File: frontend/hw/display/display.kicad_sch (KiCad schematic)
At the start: 14 parts, among them J1 Conn_01x06, J3 Conn_01x04, Q1 MMBT3904, Q2 MMBT3904, U1 ESP32-WROOM-32U, U3 CH340C, U5 AMS1117-3.3

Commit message: Start connecting display.
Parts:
- removed J3: Conn_01x04, Connector_JST:JST_PH_B4B-PH-K_1x04_P2.00mm_Vertical, symbol Connector_Generic:Conn_01x04
- removed J?: Conn_02x13_Odd_Even, symbol Connector_Generic:Conn_02x13_Odd_Even
- added J2: Conn_02x17_Odd_Even, Connector_PinHeader_2.54mm:PinHeader_2x17_P2.54mm_Vertical, symbol Connector_Generic:Conn_02x17_Odd_Even
- C2, C3: value C -> 100n
- U3: footprint Package_SO:SOIC-16_3.9x9.9mm_P1.27mm -> Housings_SOIC:SOIC-16_3.9x9.9mm_Pitch1.27mm
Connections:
- net D15: now reaches U1.27 (IO16)
- net D15: now also J2.21 (Pin_21)
- net D14: now reaches U1.28 (IO17)
- net D14: now also J2.20 (Pin_20)
- net D11: now reaches U1.31 (IO19)
- net D11: now also J2.17 (Pin_17)
- net D10: now reaches U1.33 (IO21)
- net D10: now also J2.16 (Pin_16)
- net D9: now reaches U1.36 (IO22)
- net D9: now also J2.15 (Pin_15)
- net BUZ1 renamed D13
- net D13: now also J2.19 (Pin_19)
- net ESP_RFID_TX renamed D12
- net D12: now also J2.18 (Pin_18)
- new net D8: J2.14 (Pin_14)
- no-connect marks 29 -> 32

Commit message: Add more connections.
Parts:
- U3: footprint Housings_SOIC:SOIC-16_3.9x9.9mm_Pitch1.27mm -> Package_SO:SOIC-16_3.9x9.9mm_P1.27mm
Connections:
- net BUZ2 is gone; now on net RST: U1.26 (IO4)
- net GREEN is gone; now on net RS: U1.16 (IO13)
- net RED is gone; now on net CS: U1.13 (IO14)
- net +3V3: now also J2.24 (Pin_24), J2.25 (Pin_25)
- net CS: now also J2.1 (Pin_1)
- net D8: now also U1.37 (IO23)
- net GND: now also J2.26 (Pin_26), J2.27 (Pin_27)
- net RST: now also J2.5 (Pin_5)
- net WR: now also J2.3 (Pin_3), U1.14 (IO12)
- net BL: now reaches U1.23 (IO15)
- net BL: now also J2.23 (Pin_23)
- net RD: now reaches U1.24 (IO2)
- net RD: now also J2.4 (Pin_4)
- net RS: now reaches J2.2 (Pin_2)
- net SENSE: no longer names the net of U1.8 (IO32)
- no-connect marks 32 -> 29

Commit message: Ready for routing.
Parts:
- removed J1: Conn_01x06, Connector_USB:USB_Micro-B_Molex-105017-0001, symbol Connector_Generic:Conn_01x06
- added C1: 10u, Capacitor_SMD:C_0805_2012Metric, symbol Device:C
- added C6: 47u, Capacitor_SMD:CP_Elec_10x10, symbol Device:CP
- added J1: Conn_01x04, Connector_JST:JST_XH_B4B-XH-A_1x04_P2.50mm_Vertical, symbol Connector_Generic:Conn_01x04
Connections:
- net +3V3: now also C1.1
- net +5V: now also C6.1, J1.1 (Pin_1)
- net GND: now also C1.2, C6.2, J1.4 (Pin_4)
- net at U3.6 (UD-): now also J1.3 (Pin_3)
- net at U3.5 (UD+): now also J1.2 (Pin_2)
- net MISO: now reaches U1.10 (IO25)
- net MISO: now also J2.29 (Pin_29)
- net CLK: now reaches U1.11 (IO26)
- net CLK: now also J2.34 (Pin_34)
- net T_CS: now reaches U1.12 (IO27)
- net T_CS: now also J2.33 (Pin_33)
- net MOSI: now reaches U1.8 (IO32)
- net MOSI: now also J2.30 (Pin_30)
- net PEN: now reaches U1.9 (IO33)
- net PEN: now also J2.31 (Pin_31)
- no-connect marks 29 -> 26

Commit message: Do more routing.
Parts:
- C6: footprint Capacitor_SMD:CP_Elec_10x10 -> (none)
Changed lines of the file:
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@@
       (effects (font (size 1.27 1.27)) (justify left))
     )
-    (property "Footprint" "Capacitor_SMD:CP_Elec_10x10" (id 2) (at 218.6432 92.456 0)
+    (property "Footprint" "" (id 2) (at 218.6432 92.456 0)
       (effects (font (size 1.27 1.27)) hide)
     )
@@
     )
     (path "/99a0dda6-8f49-4e3d-a67f-cf43a69b6fcf"
-      (reference "C6") (unit 1) (value "47u") (footprint "Capacitor_SMD:CP_Elec_10x10")
+      (reference "C6") (unit 1) (value "47u") (footprint "")
     )
     (path "/7125cdaa-6702-4aa3-9a8b-3bc0ebf241c0"

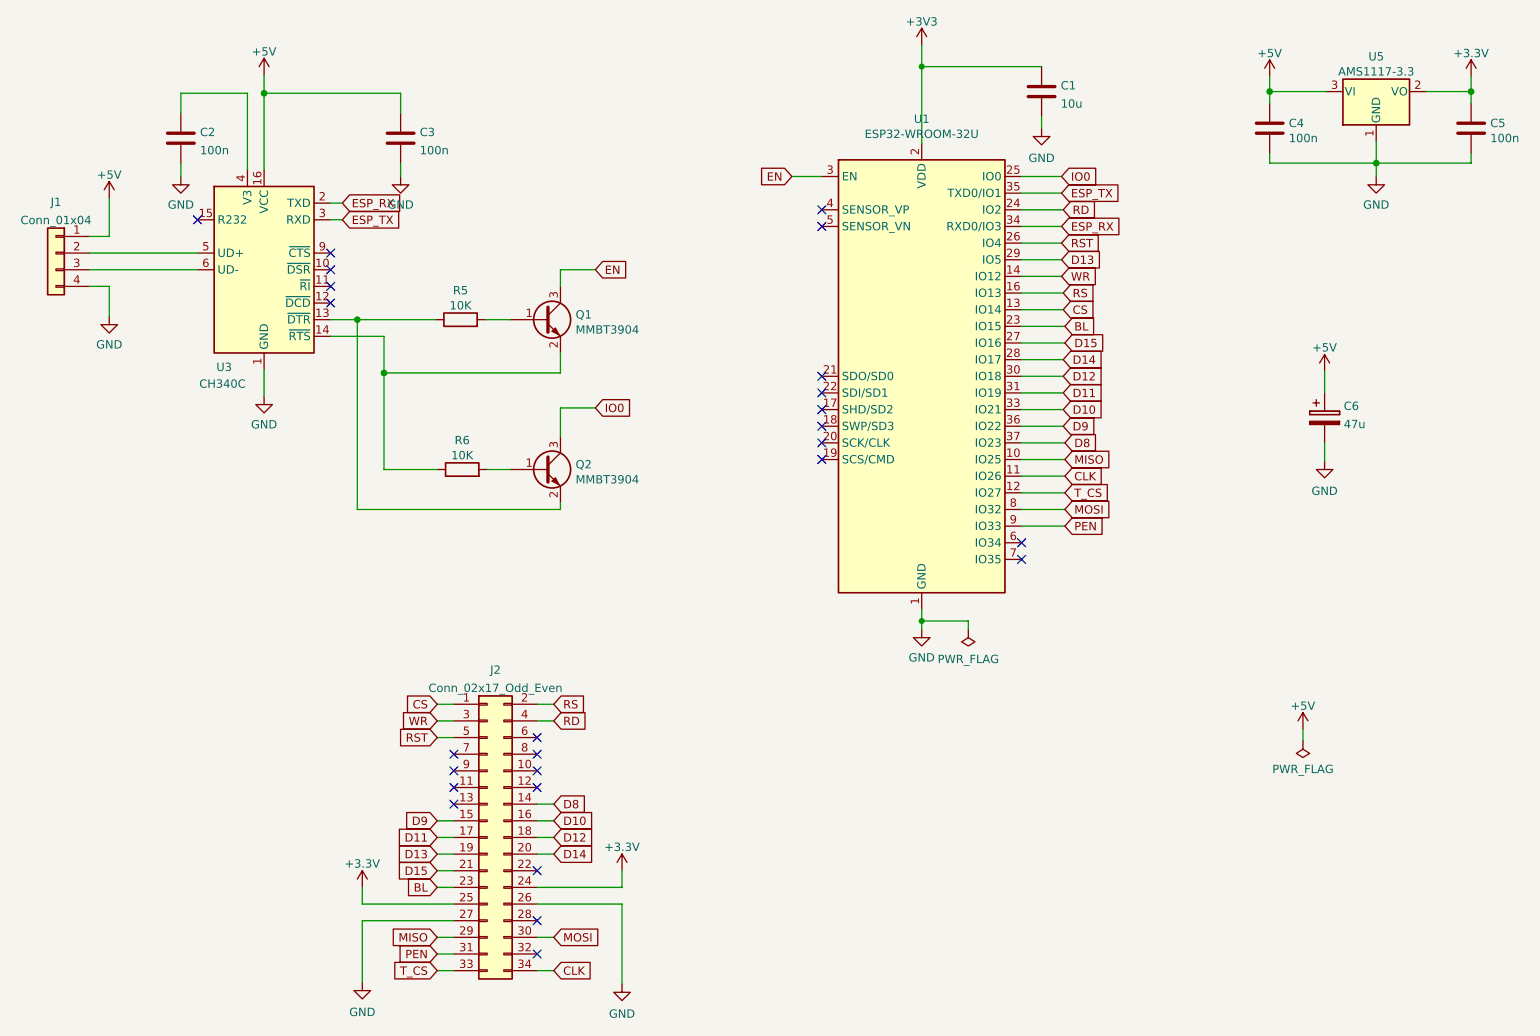
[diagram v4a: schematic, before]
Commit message: Finish routing.
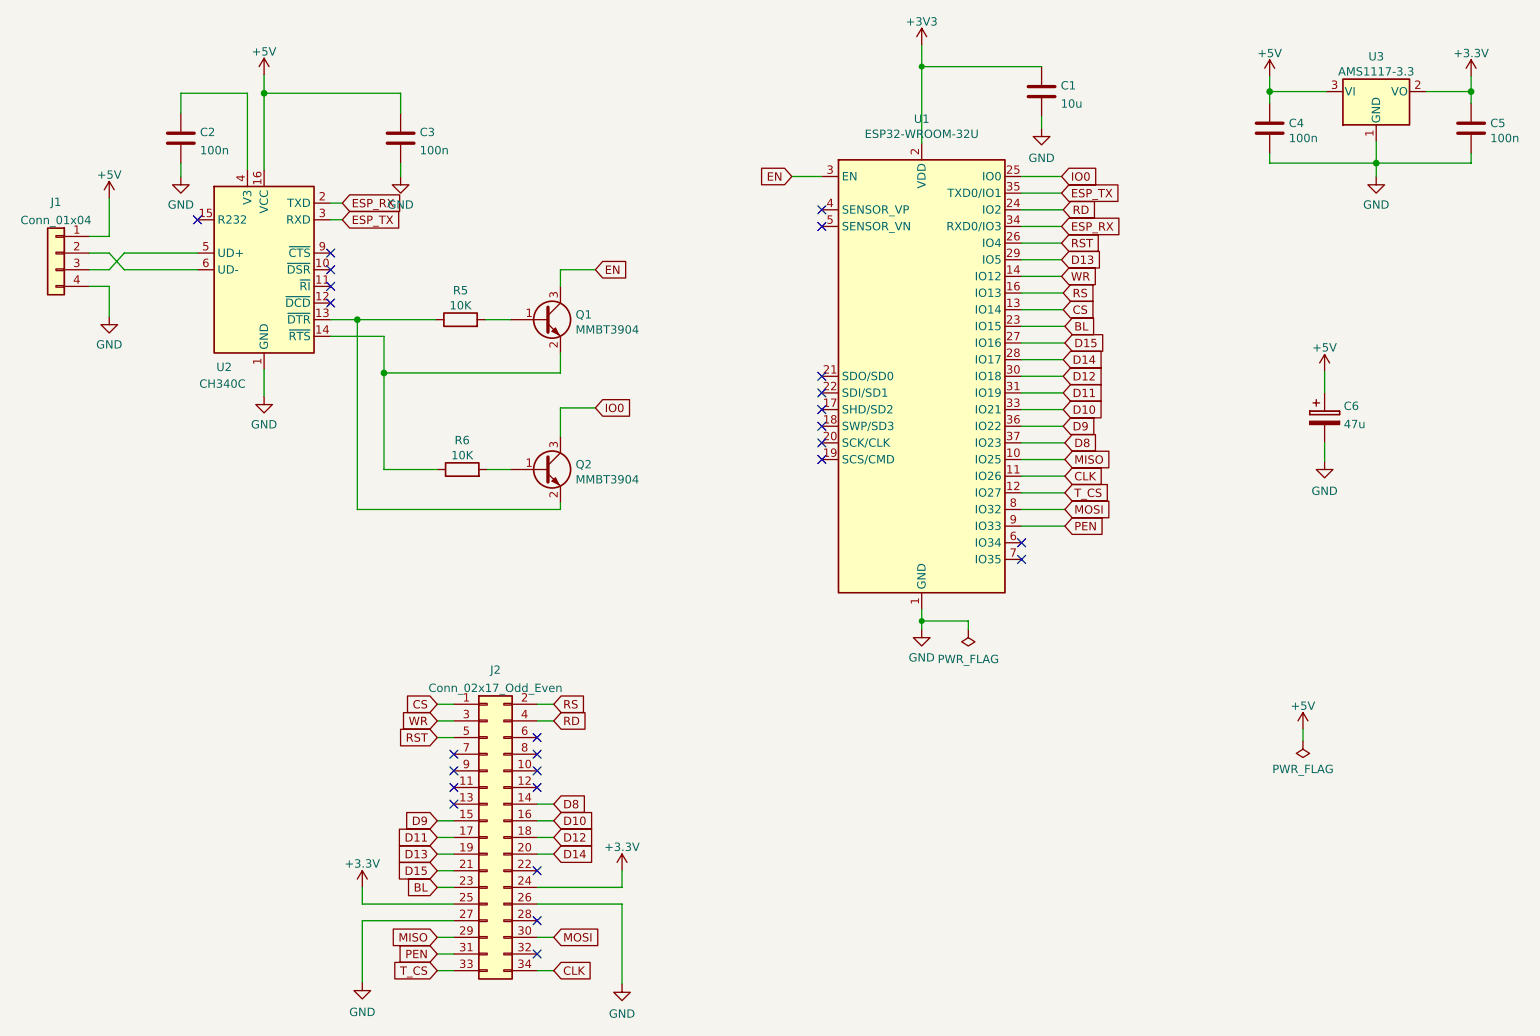
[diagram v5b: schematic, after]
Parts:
- C6: footprint (none) -> Capacitor_Tantalum_SMD:CP_EIA-7343-43_Kemet-X
- U2: renamed from U3; footprint Package_SO:SOIC-16_3.9x9.9mm_P1.27mm -> Housings_SOIC:SOIC-16_3.9x9.9mm_Pitch1.27mm
- renumbered U5 to U3
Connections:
- net at J1.2 (Pin_2): now also U2.6 (UD-); no longer U2.5 (UD+)
- net at J1.3 (Pin_3): now also U2.5 (UD+); no longer U2.6 (UD-)
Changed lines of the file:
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@@
     (stroke (width 0) (type solid) (color 0 0 0 0))
+  )
+  (wire (pts (xy 29.21 66.04) (xy 32.258 66.04))
+    (stroke (width 0) (type default) (color 0 0 0 0))
   )
   (wire (pts (xy 82.296 137.414) (xy 84.836 137.414))
@@
     (stroke (width 0) (type default) (color 0 0 0 0))
   )
+  (wire (pts (xy 34.544 63.5) (xy 45.72 63.5))
+    (stroke (width 0) (type default) (color 0 0 0 0))
+  )
   (wire (pts (xy 217.678 81.534) (xy 217.678 84.836))
     (stroke (width 0) (type default) (color 0 0 0 0))
@@
     (stroke (width 0) (type default) (color 0 0 0 0))
   )
+  (wire (pts (xy 32.258 66.04) (xy 34.544 63.5))
+    (stroke (width 0) (type default) (color 0 0 0 0))
+  )
   (wire (pts (xy 174.498 42.672) (xy 174.498 44.45))
     (stroke (width 0) (type default) (color 0 0 0 0))
@@
     (stroke (width 0) (type default) (color 0 0 0 0))
   )
-  (wire (pts (xy 29.21 63.5) (xy 45.72 63.5))
-    (stroke (width 0) (type solid) (color 0 0 0 0))
-  )
   (wire (pts (xy 171.45 94.996) (xy 178.054 94.996))
     (stroke (width 0) (type default) (color 0 0 0 0))
@@
     (stroke (width 0) (type default) (color 0 0 0 0))
   )
+  (wire (pts (xy 32.258 63.5) (xy 34.544 66.04))
+    (stroke (width 0) (type default) (color 0 0 0 0))
+  )
   (wire (pts (xy 110.49 175.006) (xy 110.49 162.814))
     (stroke (width 0) (type default) (color 0 0 0 0))
@@
     (stroke (width 0) (type default) (color 0 0 0 0))
   )
+  (wire (pts (xy 29.21 63.5) (xy 32.258 63.5))
+    (stroke (width 0) (type default) (color 0 0 0 0))
+  )
+  (wire (pts (xy 34.544 66.04) (xy 45.72 66.04))
+    (stroke (width 0) (type default) (color 0 0 0 0))
+  )
   (wire (pts (xy 156.21 35.052) (xy 156.21 46.736))
     (stroke (width 0) (type solid) (color 0 0 0 0))
@@
   )
   (wire (pts (xy 225.552 49.784) (xy 225.552 51.816))
-    (stroke (width 0) (type solid) (color 0 0 0 0))
-  )
-  (wire (pts (xy 29.21 66.04) (xy 45.72 66.04))
     (stroke (width 0) (type solid) (color 0 0 0 0))
   )
@@
   (symbol (lib_id "Interface_USB:CH340C") (at 55.88 66.04 0) (unit 1)
     (in_bom yes) (on_board yes)
-    (property "Reference" "U3" (id 0) (at 49.784 80.9054 0))
+    (property "Reference" "U2" (id 0) (at 49.784 80.9054 0))
     (property "Value" "CH340C" (id 1) (at 49.53 83.4581 0))
-    (property "Footprint" "Package_SO:SOIC-16_3.9x9.9mm_P1.27mm" (id 2) (at 57.15 80.01 0)
+    (property "Footprint" "Housings_SOIC:SOIC-16_3.9x9.9mm_Pitch1.27mm" (id 2) (at 57.15 80.01 0)
       (effects (font (size 1.27 1.27)) (justify left) hide)
     )
@@
       (effects (font (size 1.27 1.27)) (justify left))
     )
-    (property "Footprint" "" (id 2) (at 218.6432 92.456 0)
+    (property "Footprint" "Capacitor_Tantalum_SMD:CP_EIA-7343-43_Kemet-X" (id 2) (at 218.6432 92.456 0)
       (effects (font (size 1.27 1.27)) hide)
     )
@@
   (symbol (lib_id "Regulator_Linear:AMS1117-3.3") (at 225.552 38.862 0) (unit 1)
     (in_bom yes) (on_board yes) (fields_autoplaced)
-    (property "Reference" "U5" (id 0) (at 225.552 33.5238 0))
+    (property "Reference" "U3" (id 0) (at 225.552 33.5238 0))
     (property "Value" "AMS1117-3.3" (id 1) (at 225.552 35.8225 0))
     (property "Footprint" "Package_TO_SOT_SMD:SOT-223-3_TabPin2" (id 2) (at 225.552 33.782 0)
@@
     )
     (path "/99a0dda6-8f49-4e3d-a67f-cf43a69b6fcf"
-      (reference "C6") (unit 1) (value "47u") (footprint "")
+      (reference "C6") (unit 1) (value "47u") (footprint "Capacitor_Tantalum_SMD:CP_EIA-7343-43_Kemet-X")
     )
     (path "/7125cdaa-6702-4aa3-9a8b-3bc0ebf241c0"
@@
     )
     (path "/8c5522f1-c37d-4e65-acb7-e17d59f7d353"
-      (reference "U3") (unit 1) (value "CH340C") (footprint "Package_SO:SOIC-16_3.9x9.9mm_P1.27mm")
+      (reference "U2") (unit 1) (value "CH340C") (footprint "Housings_SOIC:SOIC-16_3.9x9.9mm_Pitch1.27mm")
     )
     (path "/b224048b-4b7b-41ed-93cf-7b7ec34b3b4f"
-      (reference "U5") (unit 1) (value "AMS1117-3.3") (footprint "Package_TO_SOT_SMD:SOT-223-3_TabPin2")
-    )
-  )
+      (reference "U3") (unit 1) (value "AMS1117-3.3") (footprint "Package_TO_SOT_SMD:SOT-223-3_TabPin2")
+    )
+  )

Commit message: Fix 3D view.
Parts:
- U2: footprint Housings_SOIC:SOIC-16_3.9x9.9mm_Pitch1.27mm -> Package_SO:SOIC-16_3.9x9.9mm_P1.27mm
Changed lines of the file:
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@@
     (property "Reference" "U2" (id 0) (at 49.784 80.9054 0))
     (property "Value" "CH340C" (id 1) (at 49.53 83.4581 0))
-    (property "Footprint" "Housings_SOIC:SOIC-16_3.9x9.9mm_Pitch1.27mm" (id 2) (at 57.15 80.01 0)
+    (property "Footprint" "Package_SO:SOIC-16_3.9x9.9mm_P1.27mm" (id 2) (at 57.15 80.01 0)
       (effects (font (size 1.27 1.27)) (justify left) hide)
     )
@@
     )
     (path "/8c5522f1-c37d-4e65-acb7-e17d59f7d353"
-      (reference "U2") (unit 1) (value "CH340C") (footprint "Housings_SOIC:SOIC-16_3.9x9.9mm_Pitch1.27mm")
+      (reference "U2") (unit 1) (value "CH340C") (footprint "Package_SO:SOIC-16_3.9x9.9mm_P1.27mm")
     )
     (path "/b224048b-4b7b-41ed-93cf-7b7ec34b3b4f"
